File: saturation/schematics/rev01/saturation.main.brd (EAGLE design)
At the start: 100 x 80 mm, 37 parts, among them IC1 TL084P, J1 IN, J2 OUT

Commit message: Routing for saturation
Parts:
- JP1: value (none) -> PWR
- R13: value (none) -> 10K
- R3: value (none) -> 22K
- S1: value (none) -> S1
- S2: value (none) -> S2
- S3: value (none) -> S3
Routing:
- net 0V: track 0.00 -> 183.1 mm
- net N$11: track 0.00 -> 105.8 mm
- net +12V: track 0.00 -> 103.6 mm
- net -12V: track 0.00 -> 77.7 mm, vias 0 -> 1
- net N$10: track 0.00 -> 76.3 mm
- net N$14: track 0.00 -> 44.0 mm
- net N$21: track 0.00 -> 42.7 mm
- net N$19: track 0.00 -> 40.9 mm
- net N$2: track 0.00 -> 33.7 mm
- net N$20: track 0.00 -> 33.4 mm, vias 0 -> 1
- net N$4: track 0.00 -> 30.1 mm
- net N$16: track 0.00 -> 29.6 mm
- net N$6: track 0.00 -> 27.0 mm
- net N$9: track 0.00 -> 19.9 mm
- net N$1: track 0.00 -> 16.1 mm
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- added copper zone on layer 1, net 0V
- added copper zone on layer 16, net 0V
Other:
- board size 100 x 80 mm -> 89.8 x 44.4 mm
- board text added: "saturation rev01"

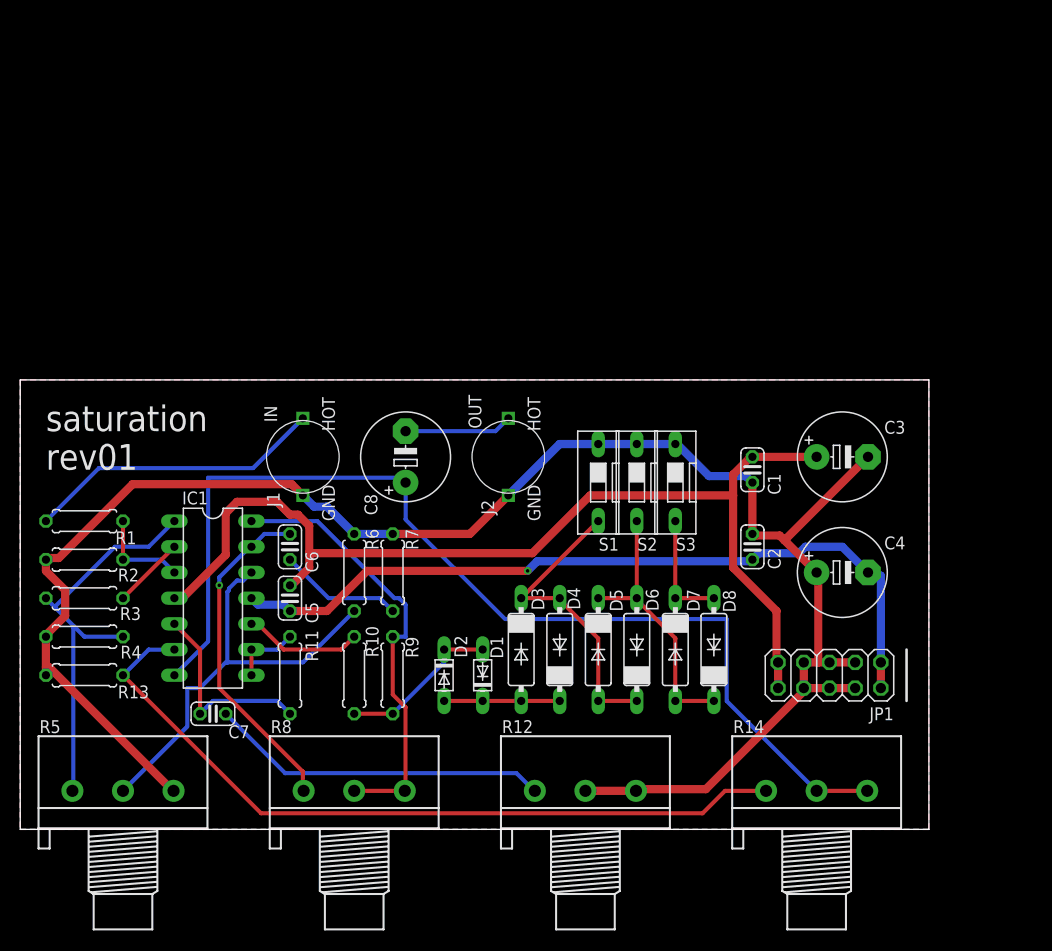
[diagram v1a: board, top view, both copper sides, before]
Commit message: Consolidate power on saturation board
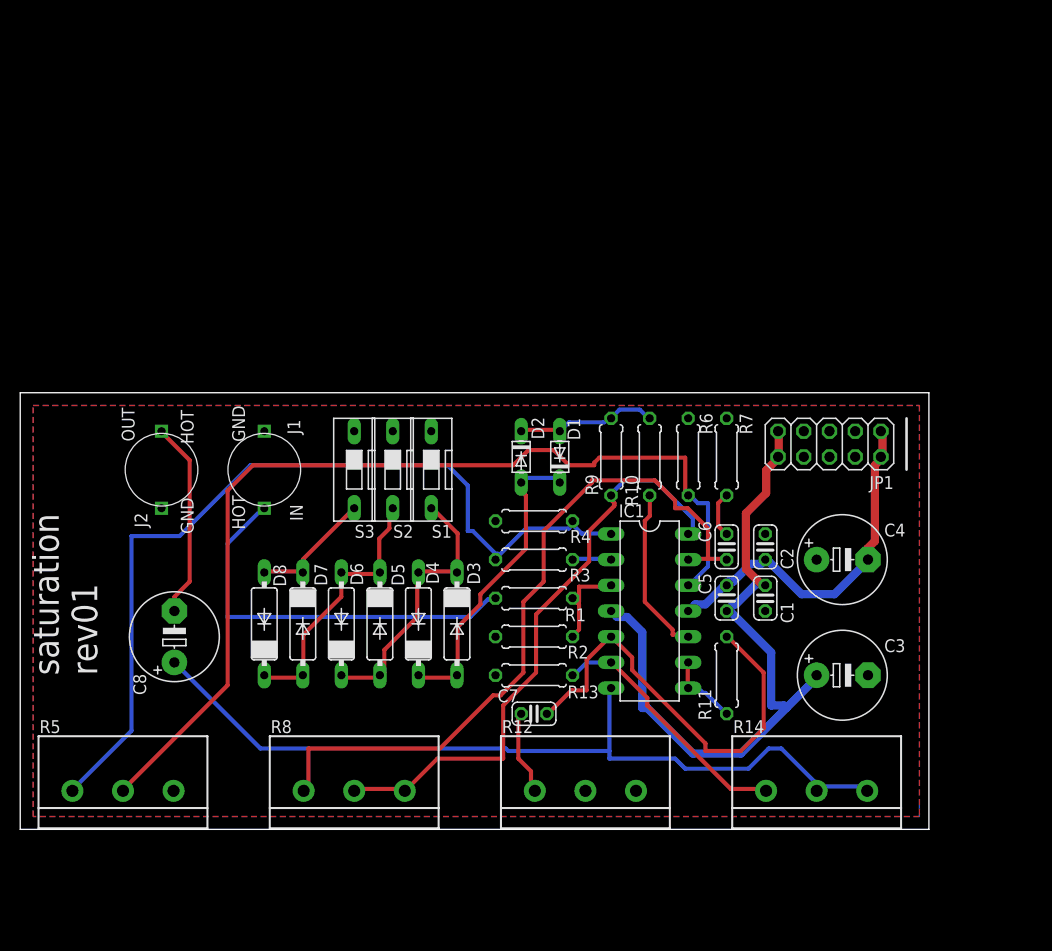
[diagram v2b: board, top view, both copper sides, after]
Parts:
- R12, R14, R5, R8: device pot:3RP/1610N -> _common:3RP/1610N
- moved R4 45.9 mm to (50.8, 30.5)
- moved R1 45.1 mm to (50.8, 22.9)
- moved R2 45.1 mm to (50.8, 19.1)
- moved R3 44.6 mm to (50.8, 26.7)
- moved D8 44.5 mm to (24.1, 20.3)
- moved R13 44.4 mm to (50.8, 15.2)
- moved IC1 43.2 mm to (62.2, 21.6)
- moved C5 43.2 mm to (69.8, 22.9), turned to 90 degrees
- moved C6 43.2 mm to (69.8, 27.9), turned to 270 degrees
- moved R11 43.2 mm to (69.8, 15.2), turned to 90 degrees
- moved D7 36.9 mm to (27.9, 20.3)
- moved R10 36.3 mm to (62.2, 36.8), turned to 270 degrees
- moved R6 34.9 mm to (66.0, 36.8)
- moved R7 34.9 mm to (69.8, 36.8)
- moved J2 34.3 mm to (14.0, 35.6)
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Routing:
- net 0V: track 183.1 -> 0.00 mm
- net N$21: track 42.7 -> 97.1 mm
- net N$10: track 76.3 -> 25.3 mm
- net N$19: track 40.9 -> 87.7 mm
- net -12V: track 77.7 -> 36.2 mm, vias 1 -> 0
- net N$20: track 33.4 -> 71.3 mm, vias 1 -> 0
- net +12V: track 103.6 -> 69.4 mm
- net N$2: track 33.7 -> 8.39 mm
- net N$9: track 19.9 -> 43.7 mm
- net N$11: track 105.8 -> 83.5 mm
- net N$3: track 11.4 -> 30.5 mm
- net N$14: track 44.0 -> 59.3 mm
- net N$16: track 29.6 -> 39.6 mm
- net N$12: track 10.7 -> 19.5 mm
- net N$15: track 12.3 -> 4.58 mm
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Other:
- board size 89.8 x 44.4 mm -> 89.8 x 43.2 mm

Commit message: Saturation schem review
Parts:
- R2: value 10K -> 22K
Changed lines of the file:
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@@
 <attribute name="VALUE" x="65.4812" y="39.116" size="1.27" layer="27" ratio="10" rot="R270"/>
 </element>
-<element name="R2" library="_common" package="0207/7" value="10K" x="50.8" y="19.05" smashed="yes">
+<element name="R2" library="_common" package="0207/7" value="22K" x="50.8" y="19.05" smashed="yes">
 <attribute name="NAME" x="54.102" y="16.891" size="1.27" layer="25" ratio="10"/>
 <attribute name="VALUE" x="48.514" y="18.4912" size="1.27" layer="27" ratio="10"/>

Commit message: Update pot values
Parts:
- R12, R14, R8: value 200K -> 200K LOG
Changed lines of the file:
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@@
 <?xml version="1.0" encoding="utf-8"?>
 <!DOCTYPE eagle SYSTEM "eagle.dtd">
-<eagle version="9.5.1">
+<eagle version="9.5.2">
 <drawing>
 <settings>
@@
 <attribute name="VALUE" x="6.985" y="6.35" size="1.27" layer="27"/>
 </element>
-<element name="R8" library="_common" package="3RP/1610N" package3d_urn="urn:adsk.eagle:package:22726/1" value="200K" x="33.02" y="3.81" smashed="yes">
+<element name="R8" library="_common" package="3RP/1610N" package3d_urn="urn:adsk.eagle:package:22726/1" value="200K LOG" x="33.02" y="3.81" smashed="yes">
 <attribute name="NAME" x="24.765" y="9.525" size="1.27" layer="25"/>
 <attribute name="POPULARITY" value="8" x="90.17" y="-10.16" size="1.778" layer="27" display="off"/>
 <attribute name="VALUE" x="29.845" y="6.35" size="1.27" layer="27"/>
 </element>
-<element name="R12" library="_common" package="3RP/1610N" package3d_urn="urn:adsk.eagle:package:22726/1" value="200K" x="55.88" y="3.81" smashed="yes">
+<element name="R12" library="_common" package="3RP/1610N" package3d_urn="urn:adsk.eagle:package:22726/1" value="200K LOG" x="55.88" y="3.81" smashed="yes">
 <attribute name="NAME" x="47.625" y="9.525" size="1.27" layer="25"/>
 <attribute name="POPULARITY" value="8" x="77.47" y="-31.75" size="1.778" layer="27" display="off"/>
@@
 <attribute name="VALUE" x="48.514" y="14.6812" size="1.27" layer="27" ratio="10"/>
 </element>
-<element name="R14" library="_common" package="3RP/1610N" package3d_urn="urn:adsk.eagle:package:22726/1" value="200K" x="78.74" y="3.81" smashed="yes">
+<element name="R14" library="_common" package="3RP/1610N" package3d_urn="urn:adsk.eagle:package:22726/1" value="200K LOG" x="78.74" y="3.81" smashed="yes">
 <attribute name="NAME" x="70.485" y="9.525" size="1.27" layer="25"/>
 <attribute name="POPULARITY" value="8" x="100.33" y="-10.16" size="1.778" layer="27" display="off"/>
